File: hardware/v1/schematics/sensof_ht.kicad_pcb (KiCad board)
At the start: 2 copper layers, 26.4 x 36.1 mm, 24 parts, among them J1 Conn_01x06, J2 Conn_01x04, U1 Si4010-GT, U2 HTU21D

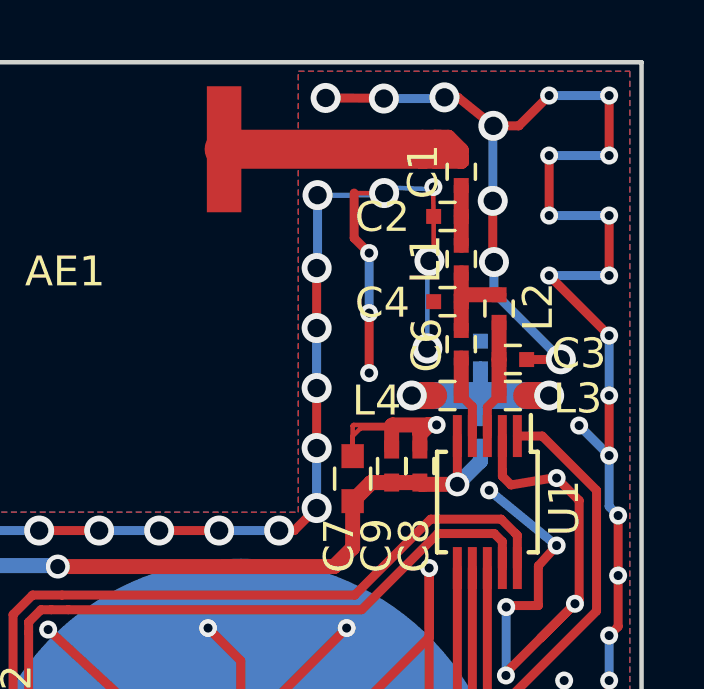
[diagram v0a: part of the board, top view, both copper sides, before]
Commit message: HW: Change fill zones and via's around matching network + add SN field
Changed the fill zones and via's to much closer resemble the Silabs
reference design. This also moves the C7/C8/C9 components.

Also added a silkscreen box where the Serial number can be written down.
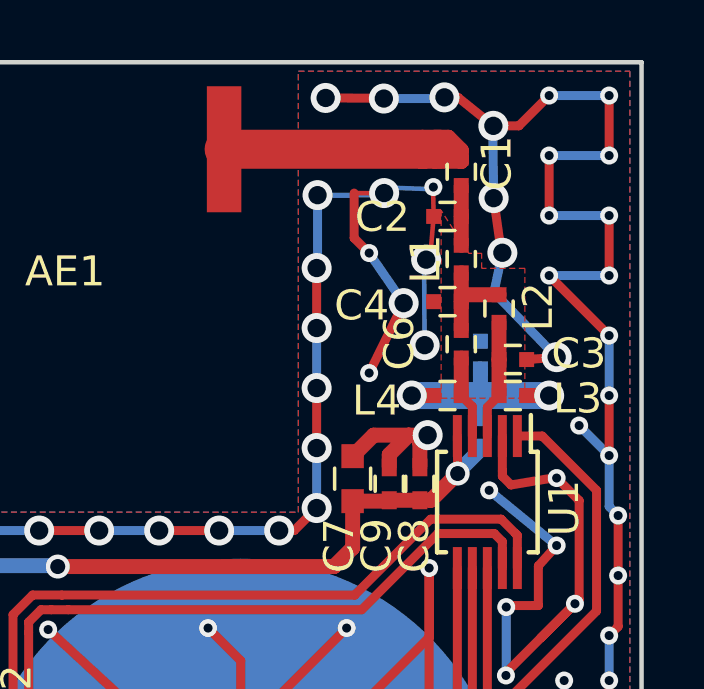
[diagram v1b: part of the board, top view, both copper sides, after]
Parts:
- moved REF** 1.22 mm to (146.3, 79.5)
- moved C9 0.60 mm to (156.5, 89.9)
- moved C8 0.59 mm to (157.5, 89.9)
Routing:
- net GND: track 352.7 -> 346.2 mm
- net VDD: track 63.7 -> 58.3 mm
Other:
- board text added: "SN:"
